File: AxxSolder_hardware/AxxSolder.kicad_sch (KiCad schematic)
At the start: 143 parts, among them IC1 TLV76733DRVR, IC2 OPA2387DSGT, IC3 LMR54406DBVR, IC4 STM32G431CBT6, IC5 TPD4E1U06DBVR, IC6 STUSB4500QTR, IC7 MAX16171ATA_VY+T, IC8 LTC4440AHMS8E, IC9 INA281A5QDBVRQ1, J1 USB4110-GF-A, J2 691243110009, J3 TSW-102-07-T-S, J4 61300611821, J5 TSW-102-07-T-S, J6 TSW-102-07-T-S, Q1 STL9P3LLH6, Q2 STL10N3LLH5, Q3 2N7002NXAKR, U2 PEC11J-9215F-S0015, U3 BSC014N04LS

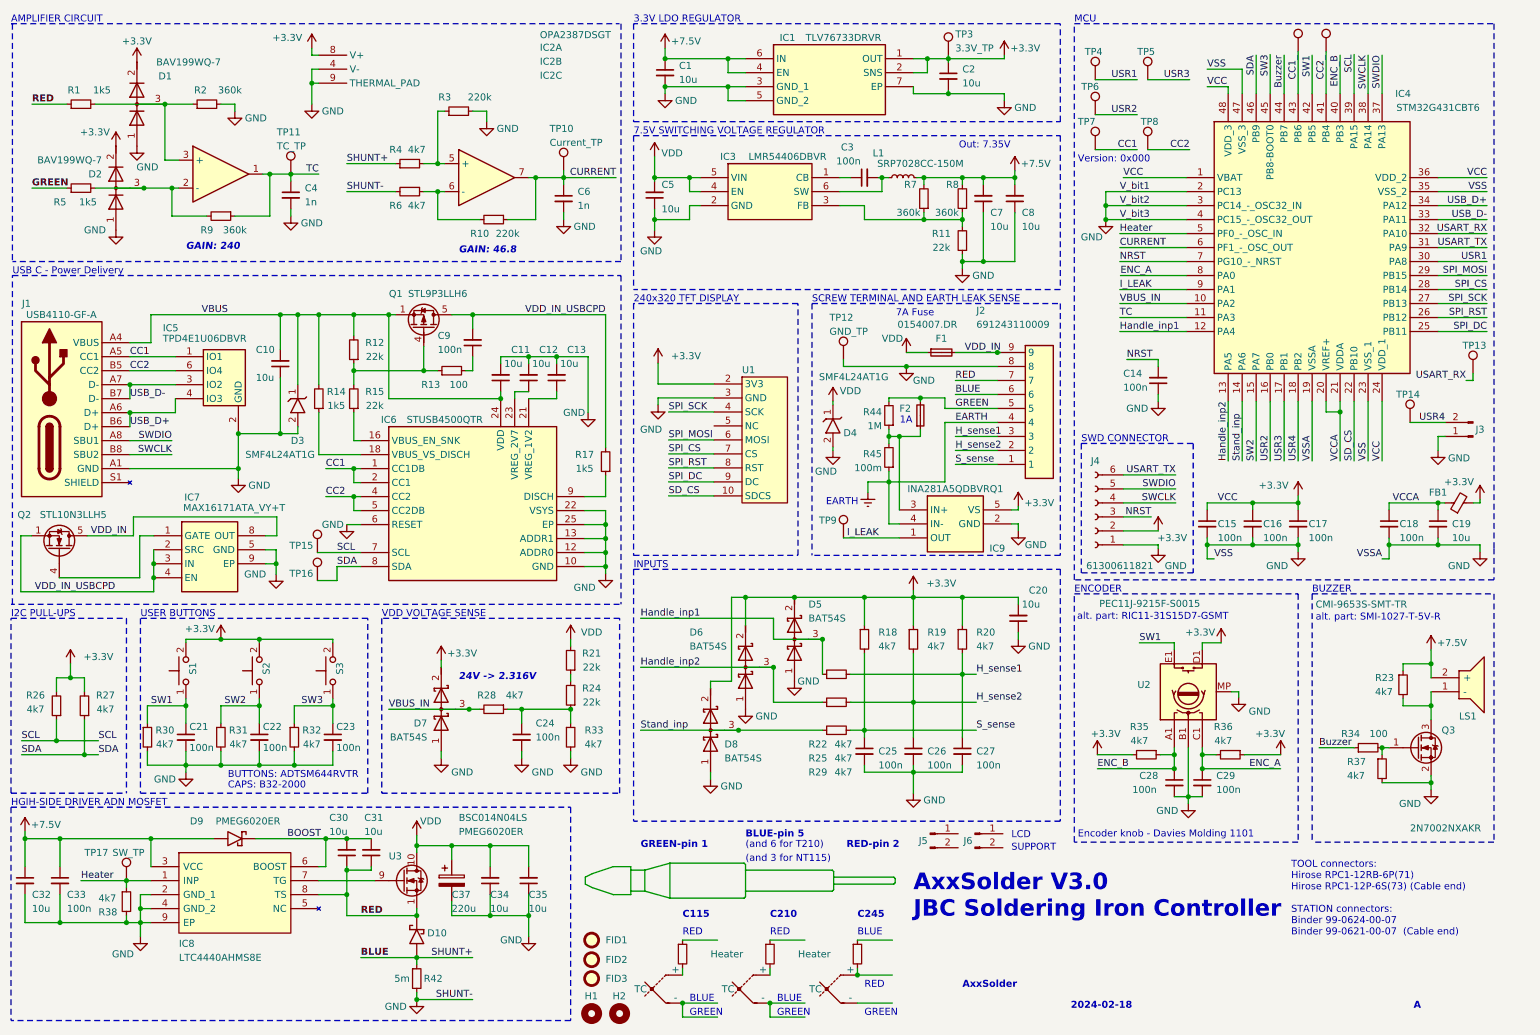
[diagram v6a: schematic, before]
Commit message: Add series resistance to button RC filters on schematic and board layout
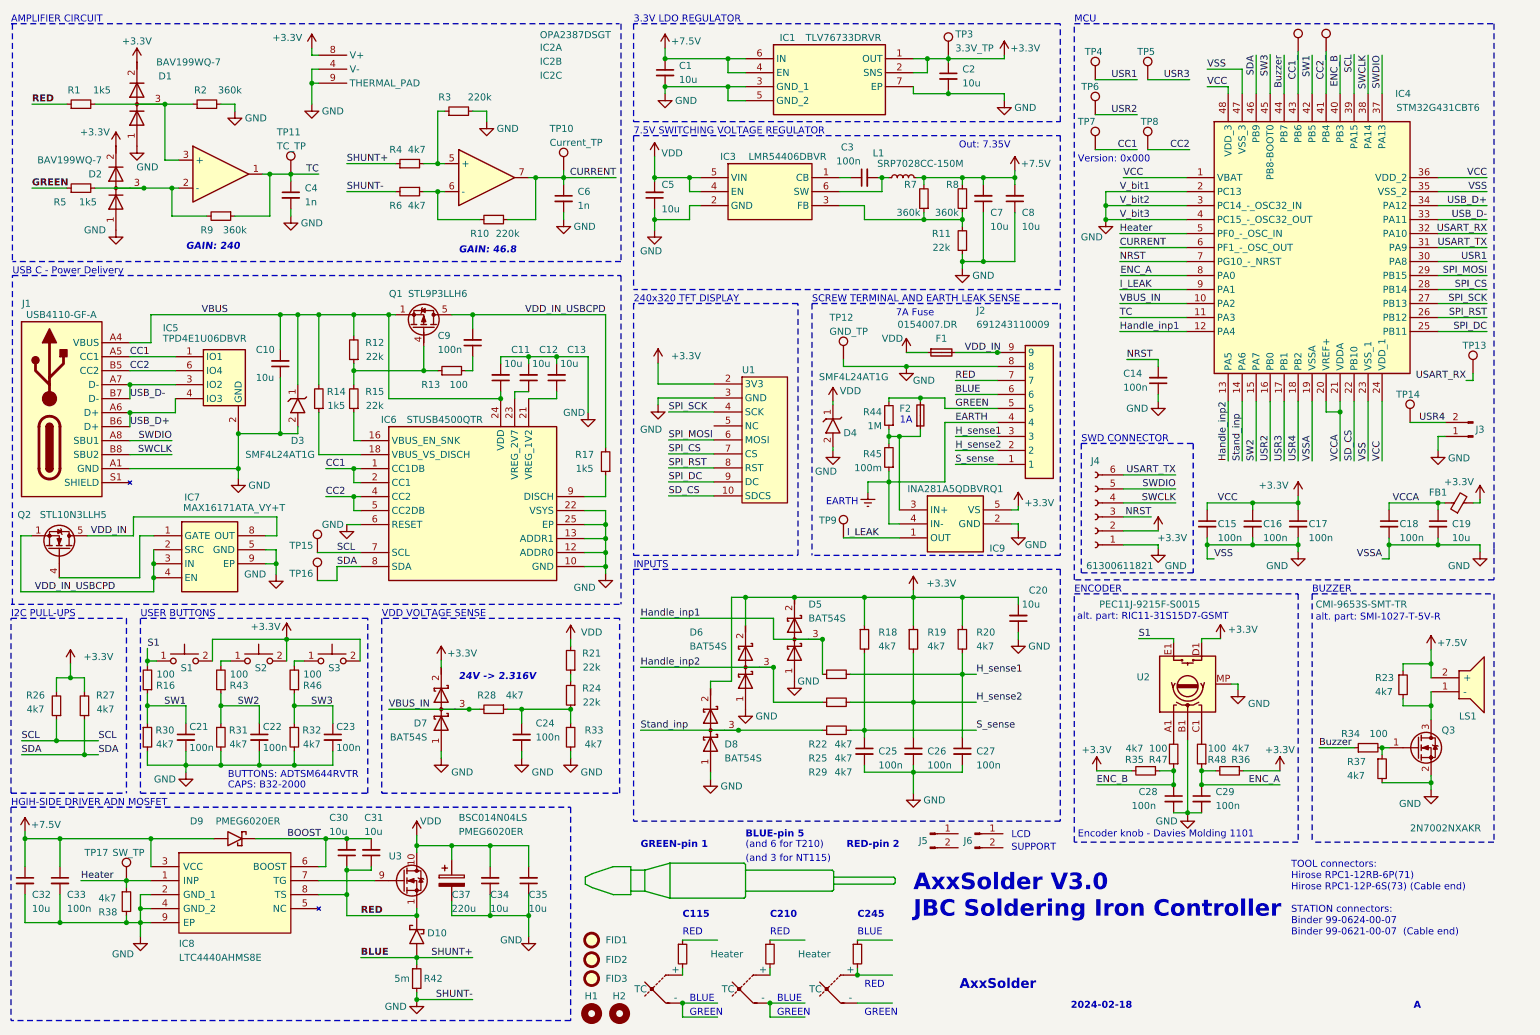
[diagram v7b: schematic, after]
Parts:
- added R16, R43, R46, R47, R48: 100, Resistor_SMD:R_0603_1608Metric, symbol Device:R_Small
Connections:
- net ENC_A: now also R48.1; no longer U2.C1
- net ENC_B: now also R47.1; no longer U2.A1
- net SW1: now also R16.1; no longer S1.1, U2.E1
- net SW2: now also R43.1; no longer S2.1
- net SW3: now also R46.1; no longer S3.1
- new net: R43.2, S2.1
- new net: R47.2, U2.A1
- new net: R48.2, U2.C1
- new net: R46.2, S3.1
- new net S1: R16.2, S1.1, U2.E1
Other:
- moved on the sheet: C28, C29, R35, R36, S1, S2, S3, U2

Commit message: Update hardware files to match correctly with current version
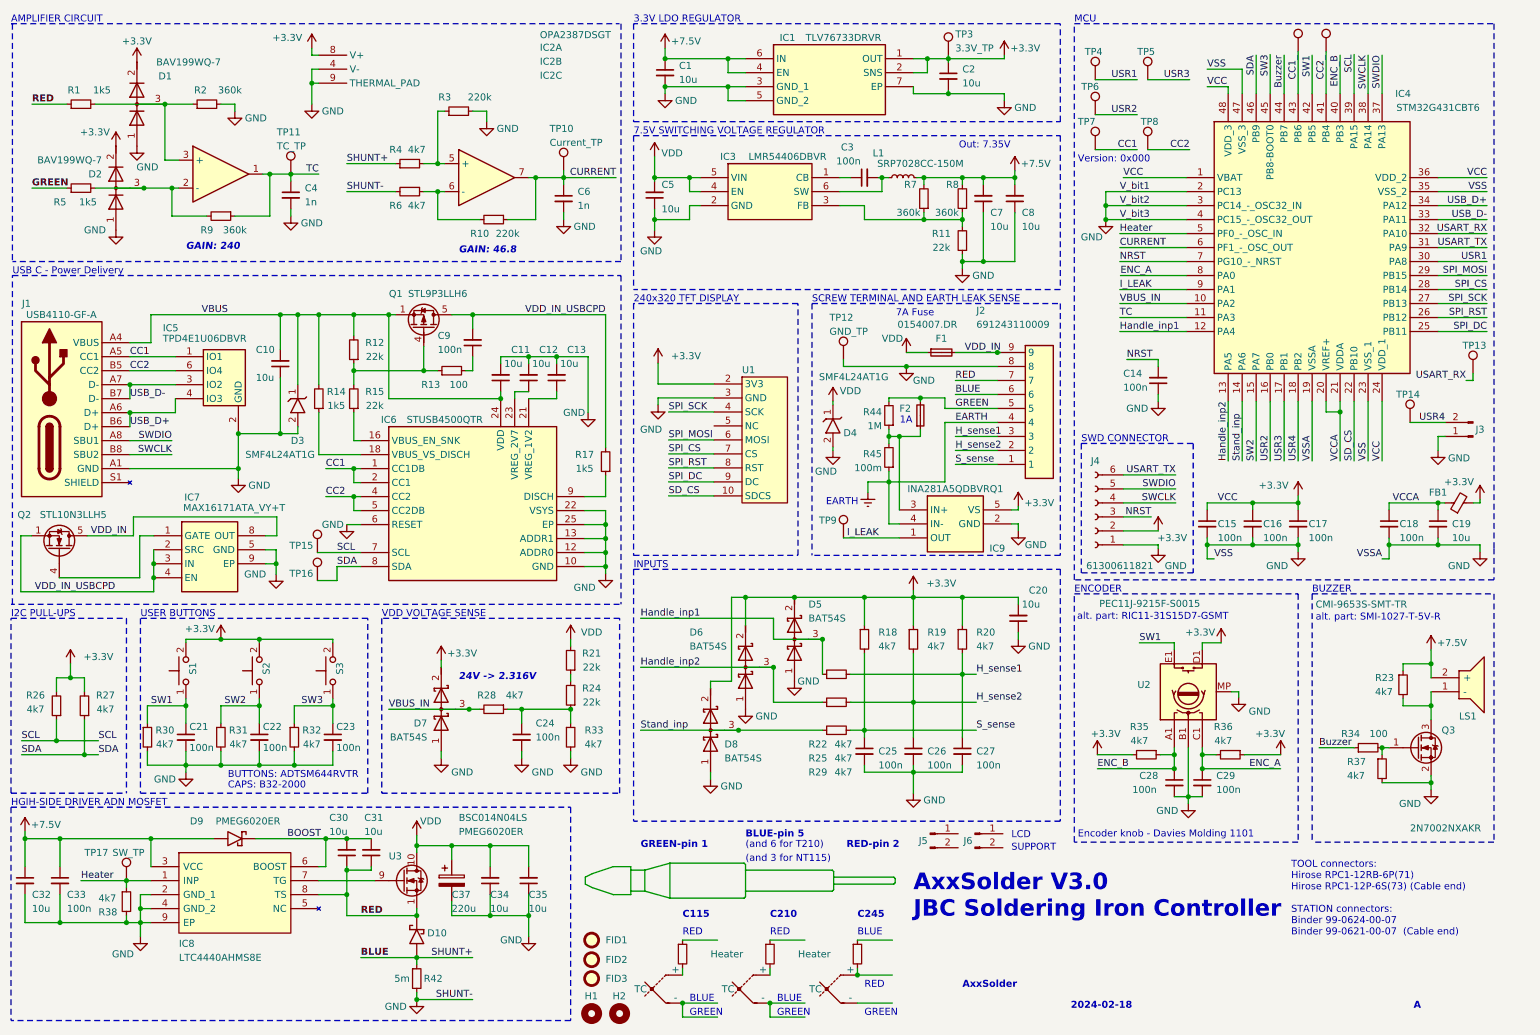
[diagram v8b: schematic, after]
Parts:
- removed R16, R43, R46, R47, R48: 100, Resistor_SMD:R_0603_1608Metric, symbol Device:R_Small
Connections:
- net S1 is gone; now on net SW1: S1.1, U2.E1
- net ENC_A: now also U2.C1
- net ENC_B: now also U2.A1
- net SW2: now also S2.1
- net SW3: now also S3.1
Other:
- moved on the sheet: C28, C29, R35, R36, S1, S2, S3, U2
